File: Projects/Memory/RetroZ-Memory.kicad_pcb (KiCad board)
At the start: 2 copper layers, 100 x 80 mm, 17 parts, among them J1 Client Bus, U1 74LS32, U2 AT28C64B-15PU, U3 74LS138, U5 74LS08, U6 AS6C4008-55PCN, U7 74HC273, U8 74LS08-And2

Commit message: sio2+ctc
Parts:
- moved REF** 0.25 mm to (107.0, 141.0)
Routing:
- net VCC: track 0.00 -> 2.54 mm
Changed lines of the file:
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@@
   (general
     (links 118)
-    (no_connects 2)
+    (no_connects 1)
     (area 106.8476 53.7126 207.592701 149.6474)
     (thickness 1.6)
     (drawings 1)
-    (tracks 903)
+    (tracks 904)
     (zones 0)
     (modules 17)
@@
   )
   (module EuroBoard_Outline:EuroBoard_halb_Type-I_100mmX80mm_holes (layer F.Cu)
-    (at 107.25 141)
+    (at 107 141)
     (descr "Outline, Eurocard 1/2, Type I, 100x80mm, with holes 3,5mm")
     (tags "Outline, Eurocard 1/2, Type I, 100x80mm, with holes 3,5mm")
@@
     (effects (font (size 1.5 1.5) (thickness 0.3)))
   )
+  (segment (start 142.24 74.93) (end 142.24 72.39) (width 0.5) (layer B.Cu) (net 1) (status C00000))
   (segment (start 123.571 120.055) (end 123.571 118.3005) (width 0.5) (layer B.Cu) (net 2))
   (segment (start 128.397 73.8505) (end 128.397 73.9775) (width 0.1524) (layer F.Cu) (net 3))

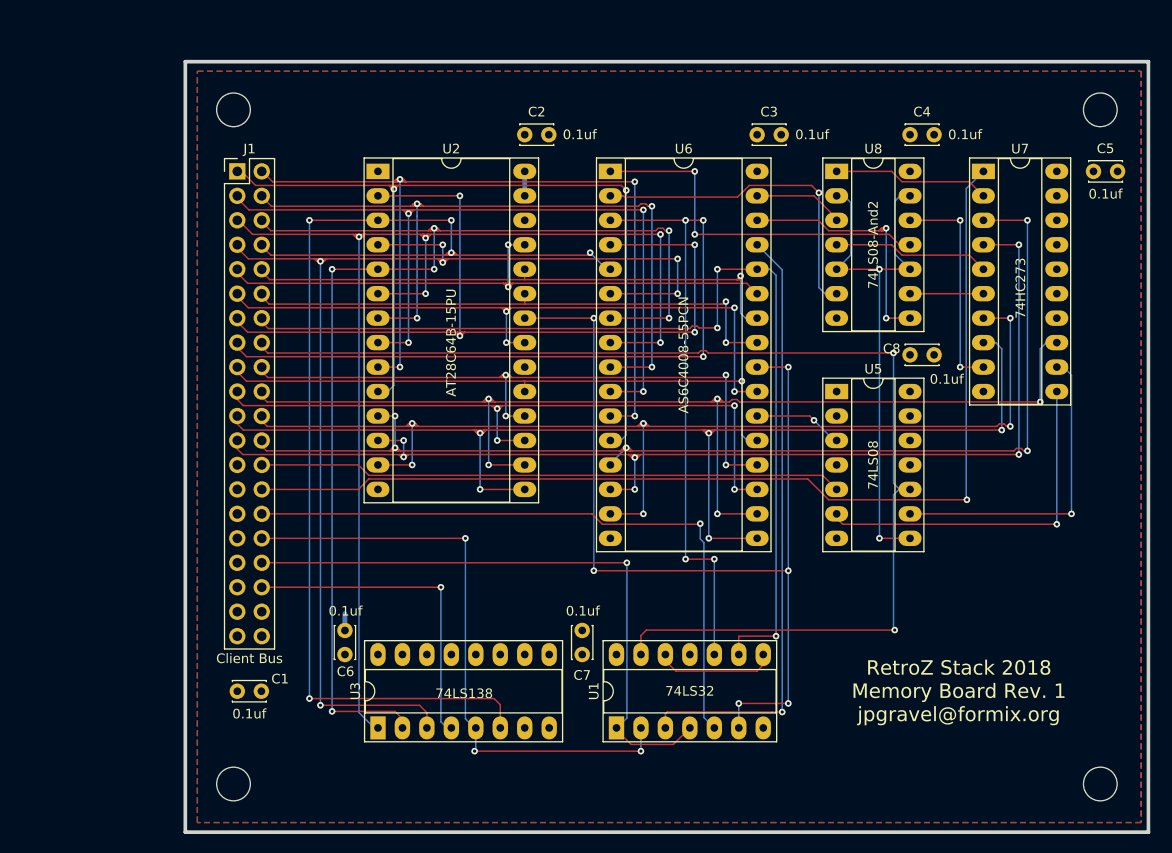
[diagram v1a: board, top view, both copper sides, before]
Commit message: added usb to serial with an FT230XS-U chip
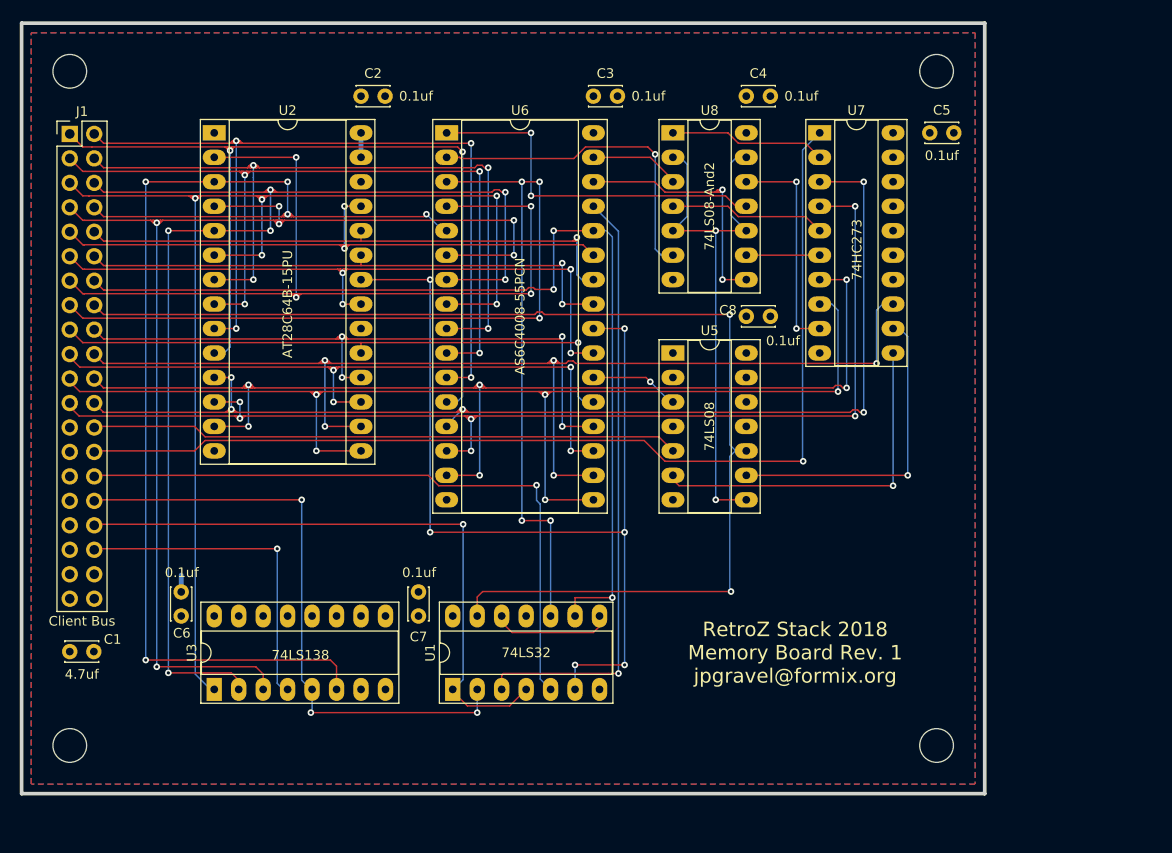
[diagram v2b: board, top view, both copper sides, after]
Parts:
- C1: value 0.1uf -> 4.7uf
- moved C1 17.9 mm to (95.0, 122.2)
- moved J1 17.8 mm to (95.0, 68.5)
- moved C2 17.5 mm to (125.2, 64.6)
- moved U1 17.5 mm to (134.8, 126.2)
- moved U3 17.5 mm to (110.0, 126.2)
- moved C3 17.5 mm to (149.4, 64.6)
- moved C4 17.5 mm to (165.2, 64.6)
- moved C5 17.5 mm to (184.3, 68.4)
- moved C6 17.5 mm to (106.6, 118.6)
- moved C7 17.5 mm to (131.2, 118.6)
- moved C8 17.5 mm to (165.2, 87.4)
- moved REF** 17.5 mm to (90.0, 137.0)
- moved U2 17.5 mm to (110.0, 68.4)
- moved U5 17.5 mm to (157.6, 91.2)
- moved U6 17.5 mm to (134.1, 68.4)
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
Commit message: in the process of updating the bus and fixing memory board mega-issue!
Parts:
- added C10: 0.1uf, Capacitors_THT:C_Disc_D3.4mm_W2.1mm_P2.50mm, F.Cu at (184.3, 112.0)
- added C9: 0.1uf, Capacitors_THT:C_Disc_D3.4mm_W2.1mm_P2.50mm, F.Cu at (169.0, 114.6)
- added U4: 74HCT04, Housings_DIP:DIP-14_W7.62mm_Socket_LongPads, F.Cu at (157.6, 114.6)
- added U9: 74LS138, Housings_DIP:DIP-16_W7.62mm_Socket_LongPads, F.Cu at (172.8, 112.0)
- U8: value 74LS08-And2 -> 74LS08
- moved C8 4.99 mm to (168.5, 91.2), turned to 90 degrees
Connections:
- net Net-(J1-Pad34) renamed ~MREQ
- J1 pad 27: Net-(J1-Pad27) -> A19
- J1 pad 29: Net-(J1-Pad29) -> A20
- J1 pad 31: Net-(J1-Pad31) -> A21
- U5 pad 3: ~RAM_SEL -> /~RAMS
- U7 pad 12: RAMONLY -> A19
- U7 pad 14: GND -> /D5
- U7 pad 15: Net-(U7-Pad15) -> A20
- U7 pad 16: Net-(U7-Pad16) -> A21
- U7 pad 17: GND -> /D6
- U7 pad 18: GND -> /D7
- U7 pad 19: Net-(U7-Pad19) -> RAMONLY
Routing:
- net /D6: track 69.8 -> 119.2 mm, vias 4 -> 6
- net /D7: track 61.9 -> 110.8 mm, vias 1 -> 5
- net /D5: track 71.6 -> 113.3 mm, vias 4 -> 6
- net RAMONLY: track 33.0 -> 50.4 mm
- net VCC: track 2.54 -> 8.11 mm, vias 0 -> 1
- net ~RAM_SEL: track 9.31 -> 6.09 mm
- net /~RAMS: track 0.00 -> 3.22 mm
- net A19: track 0.00 -> 0.70 mm

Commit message: terminated the memory board
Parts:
- C1: footprint Capacitors_THT:C_Disc_D3.4mm_W2.1mm_P2.50mm -> Capacitors_THT:CP_Radial_D5.0mm_P2.50mm
- moved C1 1.51 mm to (95.0, 123.8)
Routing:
- net A21: track 0.00 -> 134.5 mm, vias 0 -> 3
- net A20: track 0.00 -> 131.2 mm, vias 0 -> 4
- net A19: track 0.70 -> 122.6 mm, vias 0 -> 3
- net ~ROM_SEL: track 0.00 -> 80.8 mm, vias 0 -> 1
- net Net-(U3-Pad15): track 0.00 -> 52.1 mm, vias 0 -> 2
- net /~RAMS: track 3.22 -> 50.0 mm, vias 0 -> 2
- net ~RAM_SEL: track 6.09 -> 50.6 mm, vias 1 -> 3
- net Net-(U4-Pad6): track 0.00 -> 37.5 mm
- net ~MREQ: track 64.7 -> 101.0 mm, vias 1 -> 2
- net RAMONLY: track 50.4 -> 78.8 mm, vias 1 -> 3
- net Net-(U4-Pad4): track 0.00 -> 27.8 mm, vias 0 -> 2
- net Net-(U4-Pad2): track 0.00 -> 24.6 mm
- net Net-(U1-Pad11): track 0.00 -> 19.2 mm, vias 0 -> 1

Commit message: finished sio2 board
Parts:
- moved J1 0.22 mm to (94.9, 68.3)
- moved REF** 0.22 mm to (89.9, 136.8)
- moved C1 0.05 mm to (94.9, 123.8)
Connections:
- net A19 renamed DMA0
- net A20 renamed DMA1
- net A21 renamed DMA2

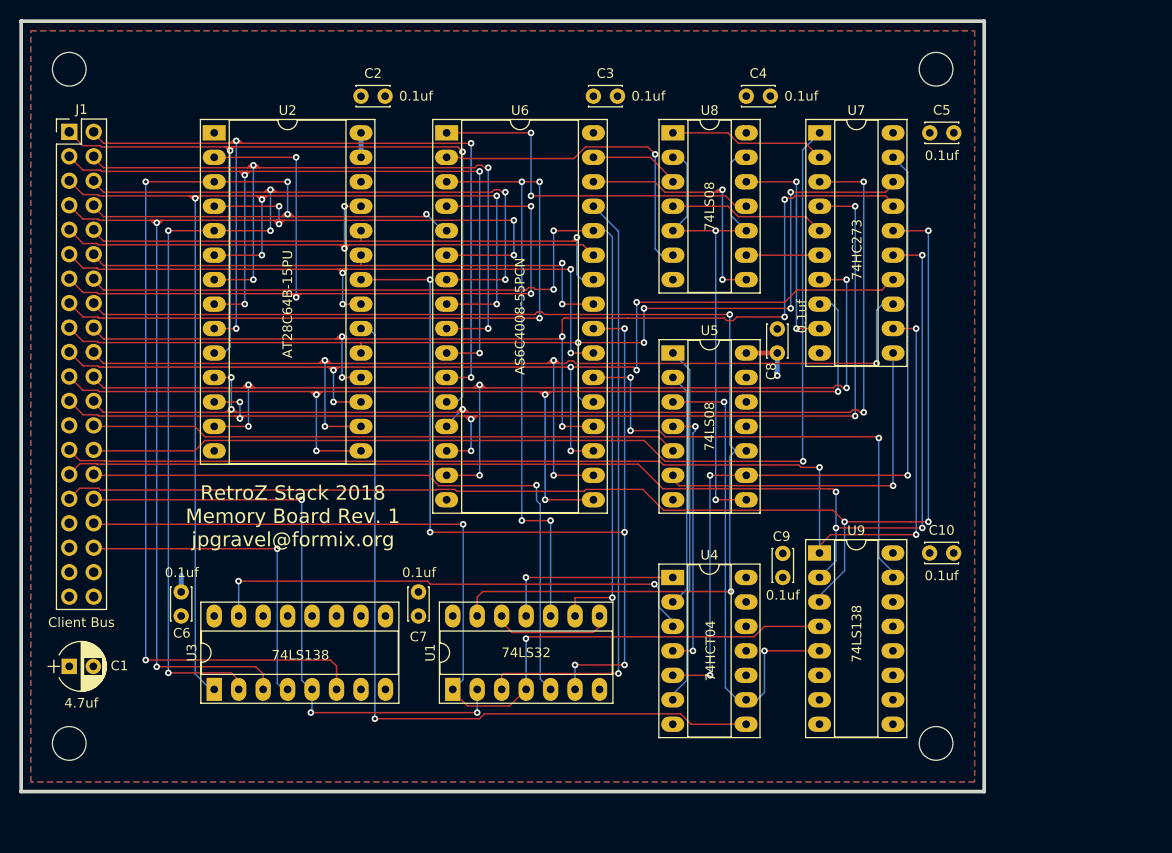
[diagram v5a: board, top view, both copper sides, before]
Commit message: fixed a bunch of issues with the main board and some on the memory board
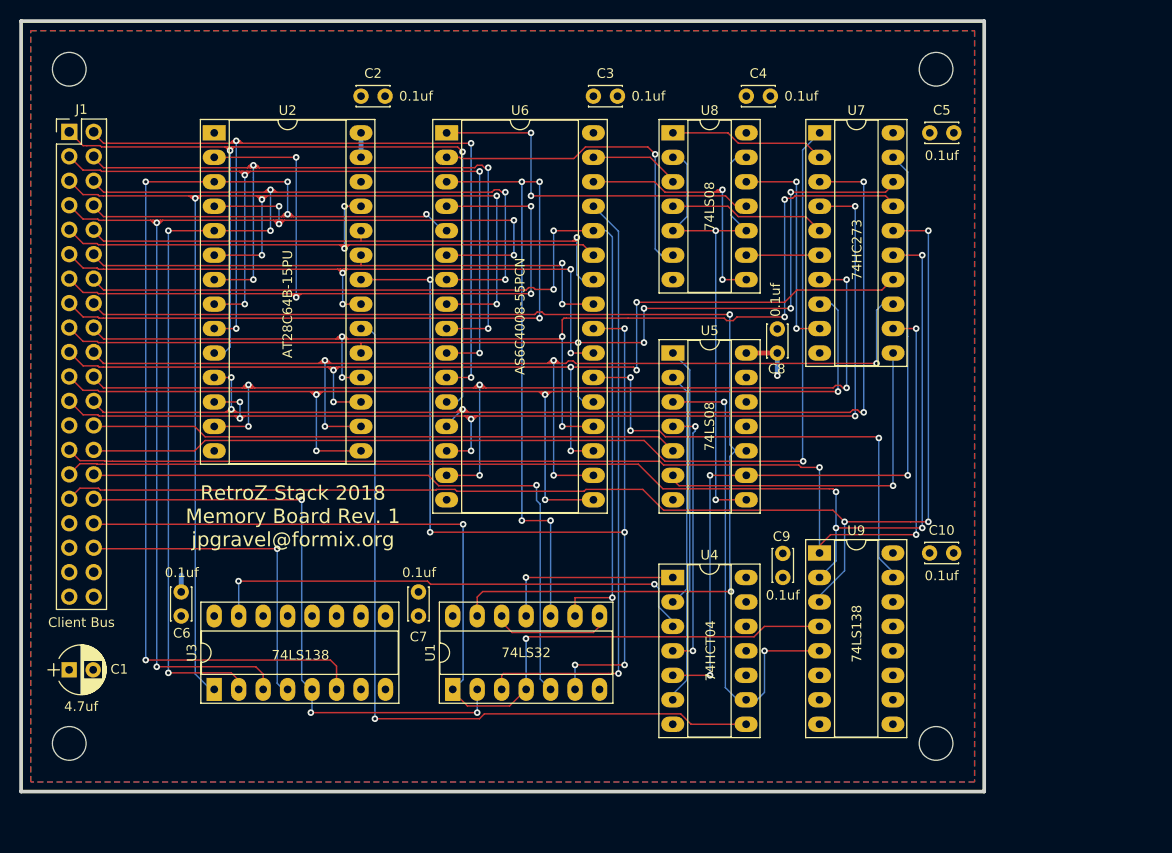
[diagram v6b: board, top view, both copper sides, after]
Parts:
- moved C1 0.36 mm to (94.9, 124.1)
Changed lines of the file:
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@@
     (links 143)
     (no_connects 0)
-    (area 89.5446 49.4981 190.289701 145.4329)
+    (area 0 0 0 0)
     (thickness 1.6)
     (drawings 1)
@@
     (descr "C, Disc series, Radial, pin pitch=2.50mm, , diameter*width=3.4*2.1mm^2, Capacitor, http://www.vishay.com/docs/45233/krseries.pdf")
     (tags "C Disc series Radial pin pitch 2.50mm  diameter 3.4mm width 2.1mm Capacitor")
-    (fp_text reference C8 (at -1.905 -0.635 90) (layer F.SilkS)
-      (effects (font (size 1 1) (thickness 0.15)))
-    )
-    (fp_text value 0.1uf (at 3.81 2.54 90) (layer F.SilkS)
+    (fp_text reference C8 (at -1.651 -0.0635 180) (layer F.SilkS)
+      (effects (font (size 1 1) (thickness 0.15)))
+    )
+    (fp_text value 0.1uf (at 5.5245 -0.1905 90) (layer F.SilkS)
       (effects (font (size 1 1) (thickness 0.15)))
     )
@@
   )
   (module Capacitors_THT:CP_Radial_D5.0mm_P2.50mm (layer F.Cu)
-    (at 94.947 123.7855)
+    (at 94.9325 124.1425)
     (descr "CP, Radial series, Radial, pin pitch=2.50mm, , diameter=5mm, Electrolytic Capacitor")
     (tags "CP Radial series Radial pin pitch 2.50mm  diameter 5mm Electrolytic Capacitor")

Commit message: fixing memory access time
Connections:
- U5 pad 11: (no net) -> /RAM_E
- U5 pad 12: (no net) -> ~RAM_SEL
- U5 pad 13: (no net) -> A15
- U6 pad 22: ~RAM_SEL -> /RAM_E
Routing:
- net /RAM_E: track 0.00 -> 22.4 mm, vias 0 -> 2
- net ~RAM_SEL: track 50.6 -> 33.6 mm, vias 3 -> 1
- net A15: track 126.7 -> 136.8 mm

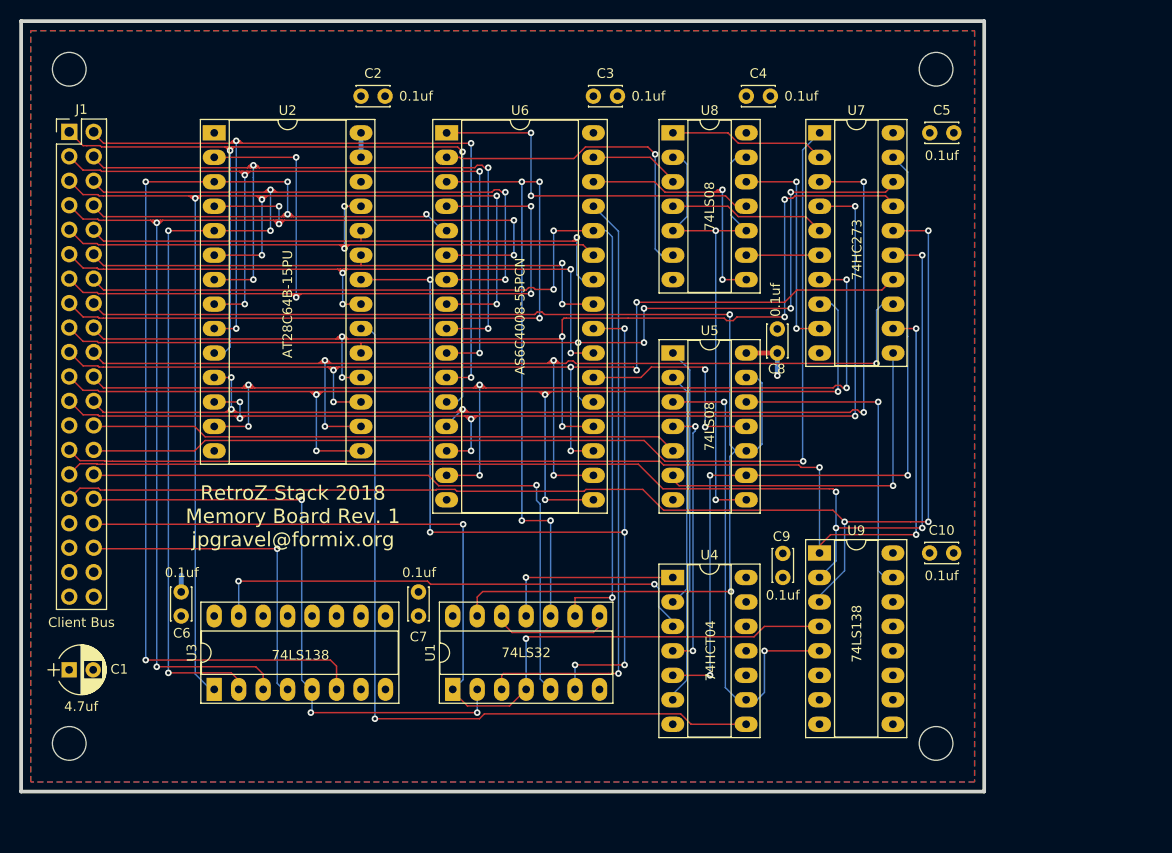
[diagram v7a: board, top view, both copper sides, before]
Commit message: added quad nor to accelerate memory chip select decoding
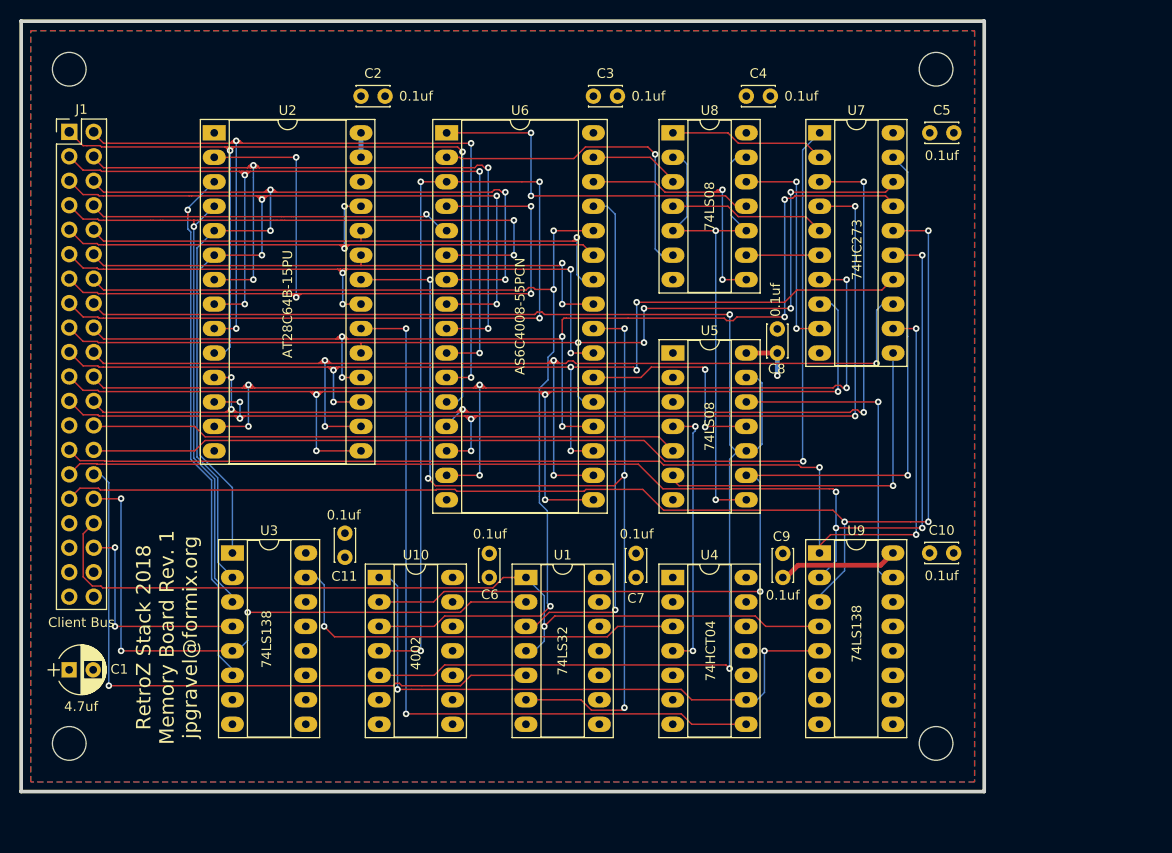
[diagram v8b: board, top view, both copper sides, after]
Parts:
- added C11: 0.1uf, Capacitors_THT:C_Disc_D3.4mm_W2.1mm_P2.50mm, F.Cu at (123.6, 112.5)
- added U10: 4002, Housings_DIP:DIP-14_W7.62mm_Socket_LongPads, F.Cu at (127.1, 114.6)
- moved C6 32.2 mm to (138.6, 114.6)
- moved C7 22.9 mm to (153.8, 114.6)
- moved U3 14.3 mm to (111.9, 112.0), turned to 0 degrees
- moved U1 13.9 mm to (142.4, 114.6), turned to 0 degrees
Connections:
- U1 pad 10: /A14 -> (no net)
- U1 pad 11: Net-(U1-Pad11) -> (no net)
- U1 pad 12: Net-(U1-Pad12) -> (no net)
- U1 pad 13: A15 -> (no net)
- U1 pad 8: Net-(U1-Pad12) -> (no net)
- U1 pad 9: /A13 -> (no net)
- U4 pad 1: Net-(U1-Pad11) -> (no net)
- U4 pad 2: Net-(U4-Pad2) -> (no net)
- U4 pad 5: RAMONLY -> (no net)
- U4 pad 6: Net-(U4-Pad6) -> (no net)
- U5 pad 1: Net-(U4-Pad6) -> (no net)
- U5 pad 2: Net-(U4-Pad2) -> (no net)
- U5 pad 3: /~RAMS -> (no net)
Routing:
- net Net-(U4-Pad6): track 37.5 -> 0.00 mm
- net /A7: track 130.2 -> 93.0 mm, vias 5 -> 2
- net /A6: track 130.1 -> 101.7 mm, vias 6 -> 3
- net RAMONLY: track 78.8 -> 103.5 mm, vias 3 -> 2
- net Net-(U4-Pad2): track 24.6 -> 0.00 mm
- net /A4: track 129.6 -> 108.6 mm, vias 5 -> 4
- net /A5: track 129.7 -> 108.8 mm, vias 6 -> 4
- net Net-(U1-Pad11): track 19.2 -> 0.00 mm, vias 1 -> 0
- net A15: track 136.8 -> 153.1 mm
- net /~RAMS: track 50.0 -> 62.8 mm
- net Net-(U1-Pad12): track 12.6 -> 0.00 mm
- net VCC: track 8.11 -> 20.6 mm
- net ~IORQ: track 33.9 -> 22.6 mm, vias 1 -> 2
- net ~MWR: track 63.3 -> 53.7 mm
- net ~MREQ: track 101.0 -> 92.1 mm, vias 2 -> 1
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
